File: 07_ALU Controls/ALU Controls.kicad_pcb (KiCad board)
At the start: 2 copper layers, 100 x 100 mm, 31 parts, among them J1 Operators 1, J2 Operators 2, J3 Operand, J4 Data Bus, J5 Alu-Out Bus, J6 Input 1, J7 Input 2, U1 74LS138, U2 74LS138, U3 74LS139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

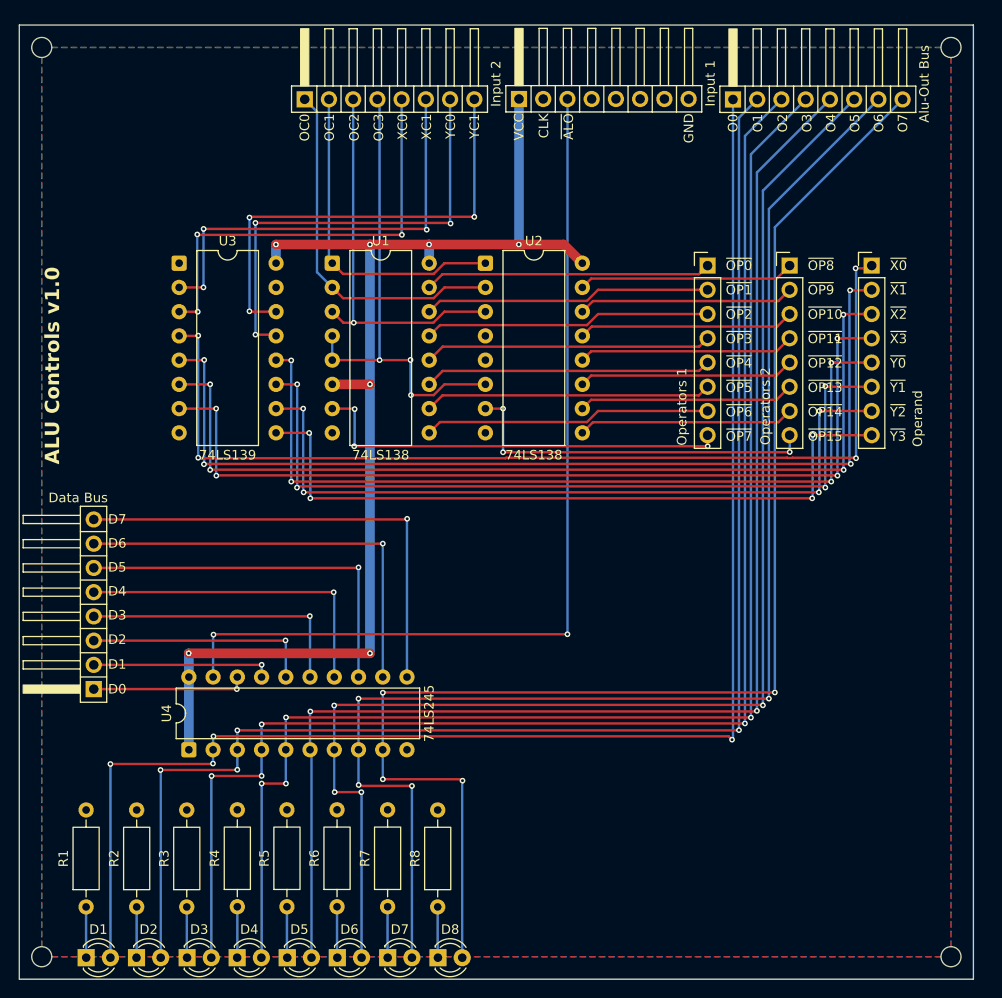
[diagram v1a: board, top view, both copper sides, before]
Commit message: Last revision of the cpu, all boards have been ordered. Implementation to be tested and documented in following commits.
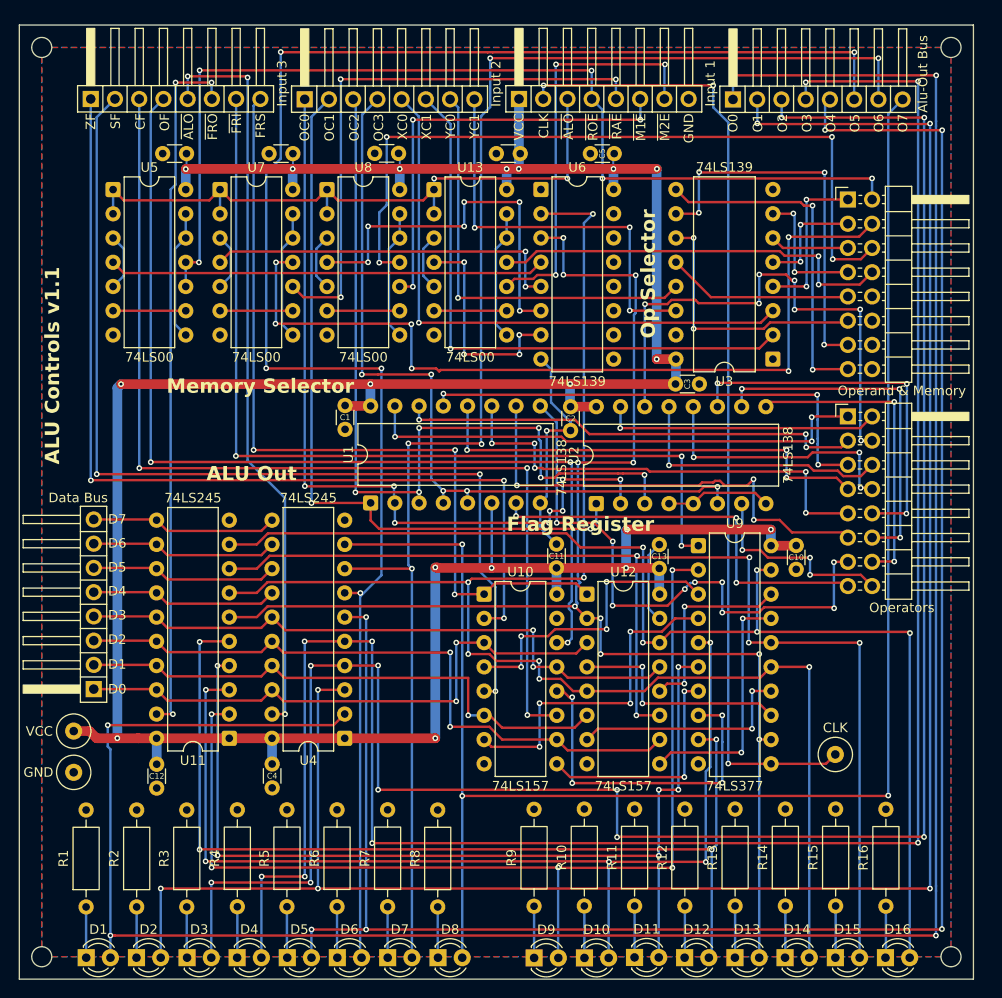
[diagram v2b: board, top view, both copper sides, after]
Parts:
- removed the J3 at (139.1, 75.1)
- added C1: 100n, Capacitor_THT:C_Disc_D3.0mm_W1.6mm_P2.50mm, F.Cu at (83.9, 89.7)
- added C10: 100n, Capacitor_THT:C_Disc_D3.0mm_W1.6mm_P2.50mm, F.Cu at (131.2, 104.4)
- added C11: 100n, Capacitor_THT:C_Disc_D3.0mm_W1.6mm_P2.50mm, F.Cu at (106.0, 106.8)
- added C12: 100n, Capacitor_THT:C_Disc_D3.0mm_W1.6mm_P2.50mm, F.Cu at (64.2, 127.3)
- added C13: 100n, Capacitor_THT:C_Disc_D3.0mm_W1.6mm_P2.50mm, F.Cu at (116.8, 106.8)
- added C2: 100n, Capacitor_THT:C_Disc_D3.0mm_W1.6mm_P2.50mm, F.Cu at (107.5, 89.8)
- added C3: 100n, Capacitor_THT:C_Disc_D3.0mm_W1.6mm_P2.50mm, F.Cu at (118.5, 87.5)
- added C4: 100n, Capacitor_THT:C_Disc_D3.0mm_W1.6mm_P2.50mm, F.Cu at (76.2, 127.3)
- added C5: 100n, Capacitor_THT:C_Disc_D3.0mm_W1.6mm_P2.50mm, F.Cu at (112.1, 63.3)
- added C6: 100n, Capacitor_THT:C_Disc_D3.0mm_W1.6mm_P2.50mm, F.Cu at (67.3, 63.3)
- added C7: 100n, Capacitor_THT:C_Disc_D3.0mm_W1.6mm_P2.50mm, F.Cu at (78.4, 63.3)
- added C8: 100n, Capacitor_THT:C_Disc_D3.0mm_W1.6mm_P2.50mm, F.Cu at (89.5, 63.3)
- added C9: 100n, Capacitor_THT:C_Disc_D3.0mm_W1.6mm_P2.50mm, F.Cu at (102.2, 63.3)
- added D10: ORA, LED_THT:LED_D3.0mm, F.Cu at (109.0, 147.6)
- added D11: ORA, LED_THT:LED_D3.0mm, F.Cu at (114.2, 147.6)
- added D12: ORA, LED_THT:LED_D3.0mm, F.Cu at (119.5, 147.6)
- added D13: ORA, LED_THT:LED_D3.0mm, F.Cu at (124.8, 147.6)
- added D14: ORA, LED_THT:LED_D3.0mm, F.Cu at (130.0, 147.6)
- added D15: ORA, LED_THT:LED_D3.0mm, F.Cu at (135.3, 147.6)
- added D16: ORA, LED_THT:LED_D3.0mm, F.Cu at (140.5, 147.6)
- added D9: ORA, LED_THT:LED_D3.0mm, F.Cu at (103.7, 147.6)
- added J7: Input 3, Custom:PinHeader_1x08_P2.54mm_Horizontal, F.Cu at (57.2, 60.4)
- added R10: 220, Resistor_THT:R_Axial_DIN0207_L6.3mm_D2.5mm_P10.16mm_Horizontal, F.Cu at (109.0, 142.2)
- added R11: 220, Resistor_THT:R_Axial_DIN0207_L6.3mm_D2.5mm_P10.16mm_Horizontal, F.Cu at (114.2, 142.2)
- added R12: 220, Resistor_THT:R_Axial_DIN0207_L6.3mm_D2.5mm_P10.16mm_Horizontal, F.Cu at (119.5, 142.2)
- added R13: 220, Resistor_THT:R_Axial_DIN0207_L6.3mm_D2.5mm_P10.16mm_Horizontal, F.Cu at (124.8, 142.2)
- added R14: 220, Resistor_THT:R_Axial_DIN0207_L6.3mm_D2.5mm_P10.16mm_Horizontal, F.Cu at (130.0, 142.2)
- added R15: 220, Resistor_THT:R_Axial_DIN0207_L6.3mm_D2.5mm_P10.16mm_Horizontal, F.Cu at (135.3, 142.2)
- added R16: 220, Resistor_THT:R_Axial_DIN0207_L6.3mm_D2.5mm_P10.16mm_Horizontal, F.Cu at (140.6, 142.2)
- added R9: 220, Resistor_THT:R_Axial_DIN0207_L6.3mm_D2.5mm_P10.16mm_Horizontal, F.Cu at (103.7, 142.2)
- added TP1: VCC, TestPoint:TestPoint_Loop_D3.50mm_Drill0.9mm_Beaded, F.Cu at (55.5, 123.8)
- added TP2: CLK, TestPoint:TestPoint_Loop_D3.50mm_Drill0.9mm_Beaded, F.Cu at (135.3, 126.3)
- added TP3: GND, TestPoint:TestPoint_Loop_D3.50mm_Drill0.9mm_Beaded, F.Cu at (55.5, 128.2)
- added U10: 74LS157, Package_DIP:DIP-16_W7.62mm, F.Cu at (98.5, 109.5)
- added U11: 74LS245, Package_DIP:DIP-20_W7.62mm, F.Cu at (71.8, 124.6)
- added U12: 74LS157, Package_DIP:DIP-16_W7.62mm, F.Cu at (109.2, 109.5)
- added U13: 74LS00, Package_DIP:DIP-14_W7.62mm, F.Cu at (93.2, 67.1)
- added U5: 74LS00, Package_DIP:DIP-14_W7.62mm, F.Cu at (59.6, 67.1)
- added U6: 74LS139, Package_DIP:DIP-16_W7.62mm, F.Cu at (104.4, 67.1)
- added U7: 74LS00, Package_DIP:DIP-14_W7.62mm, F.Cu at (70.8, 67.1)
- added U8: 74LS00, Package_DIP:DIP-14_W7.62mm, F.Cu at (82.0, 67.1)
- added U9: 74LS377, Package_DIP:DIP-20_W7.62mm, F.Cu at (120.9, 104.4)
- J1: value Operators 1 -> Operators; footprint Custom:PinHeader_1x08_P2.54mm_Vertical -> Connector_PinHeader_2.54mm:PinHeader_2x08_P2.54mm_Horizontal
- J2: value Operators 2 -> Operand & Memory; footprint Custom:PinHeader_1x08_P2.54mm_Vertical -> Connector_PinHeader_2.54mm:PinHeader_2x08_P2.54mm_Horizontal
- moved U3 63.0 mm to (128.7, 84.9), turned to 180 degrees
- moved U2 27.8 mm to (110.2, 100.0), turned to 90 degrees
- moved U1 25.4 mm to (86.6, 99.9), turned to 90 degrees
- moved J1 21.6 mm to (136.6, 90.9)
- moved U4 16.4 mm to (83.9, 124.6), turned to 180 degrees
- moved J2 9.23 mm to (136.6, 68.1)
- renumbered J4 to J3, J5 to J4, J6 to J5, J7 to J6
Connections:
- J1 pad 2: ~{OP1} -> ~{OP8}
- J1 pad 3: ~{OP2} -> ~{OP1}
- J1 pad 4: ~{OP3} -> ~{OP9}
- J1 pad 5: ~{OP4} -> ~{OP2}
- J1 pad 6: ~{OP5} -> ~{OP10}
- J1 pad 7: ~{OP6} -> ~{OP3}
- J1 pad 8: ~{OP7} -> ~{OP11}
- J2 pad 1: ~{OP8} -> ~{X0}
- J2 pad 2: ~{OP9} -> ~{ROE}
- J2 pad 3: ~{OP10} -> ~{X1}
- J2 pad 4: ~{OP11} -> ~{RAO}
- J2 pad 5: ~{OP12} -> ~{X2}
- J2 pad 6: ~{OP13} -> ~{M1O}
- J2 pad 7: ~{OP14} -> ~{X3}
- J2 pad 8: ~{OP15} -> ~{M2O}
- J5 pad 3: ~{ALO} -> ~{MIO}
- J5 pad 4: unconnected-(J6-Pin_4-Pad4) -> ~{ROE}
- J5 pad 5: unconnected-(J6-Pin_5-Pad5) -> ~{RAE}
- J5 pad 6: unconnected-(J6-Pin_6-Pad6) -> ~{M1E}
- J5 pad 7: unconnected-(J6-Pin_7-Pad7) -> ~{M2E}
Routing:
- net VCC: track 128.0 -> 324.4 mm, vias 7 -> 18
- net F5: track 0.00 -> 159.3 mm, vias 0 -> 7
- net F4: track 0.00 -> 148.2 mm, vias 0 -> 10
- net F6: track 0.00 -> 127.9 mm, vias 0 -> 5
- net F7: track 0.00 -> 125.0 mm, vias 0 -> 5
- net F0: track 0.00 -> 109.7 mm, vias 0 -> 5
- net CARRY: track 0.00 -> 108.4 mm, vias 0 -> 3
- net F1: track 0.00 -> 107.4 mm, vias 0 -> 5
- net ~{ROE}: track 0.00 -> 107.4 mm, vias 0 -> 5
- net SIGN: track 0.00 -> 104.9 mm, vias 0 -> 3
- net F3: track 0.00 -> 103.7 mm, vias 0 -> 4
- net OVER: track 0.00 -> 103.2 mm, vias 0 -> 3
- net CLK: track 0.00 -> 102.6 mm, vias 0 -> 3
- net F2: track 0.00 -> 102.0 mm, vias 0 -> 6
- net ZERO: track 0.00 -> 99.8 mm, vias 0 -> 3
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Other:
- board text added: "ALU Controls v1.1"
- board text added: "ALU Out"
- board text added: "Flag Register"
- board text added: "Memory Selector"
- board text added: "Op Selector"
- board text removed: "ALU Controls v1.0"
